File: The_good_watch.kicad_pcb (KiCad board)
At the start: 2 copper layers, 45 x 45 mm, 38 parts, among them IC1 DW01A, J1 Main, J2 USB_C_Receptacle_USB2.0, J3 PROG, J4 Screen, J5 Button, M1 Motor_DC, Q1 FS8205A, SW1 SW_Push, SW2 SW_Push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

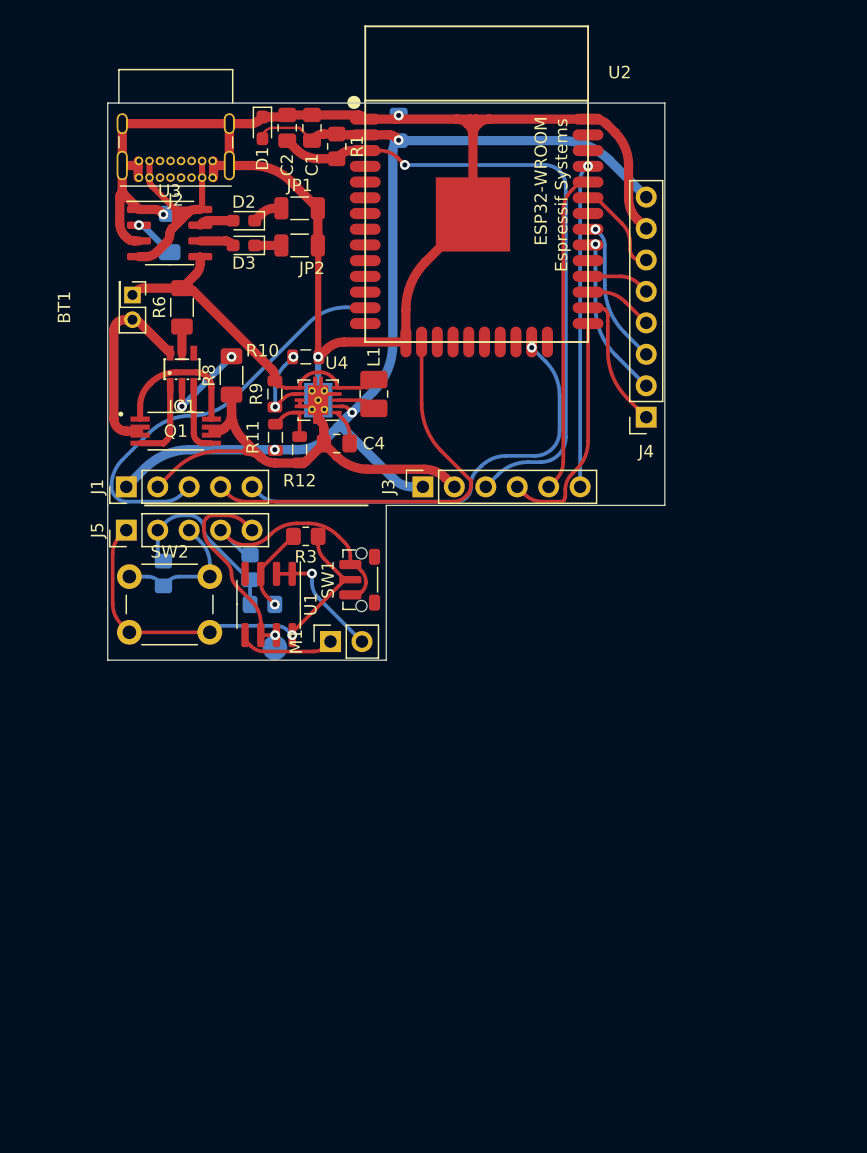
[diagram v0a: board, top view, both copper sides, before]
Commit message: Connector layout trial
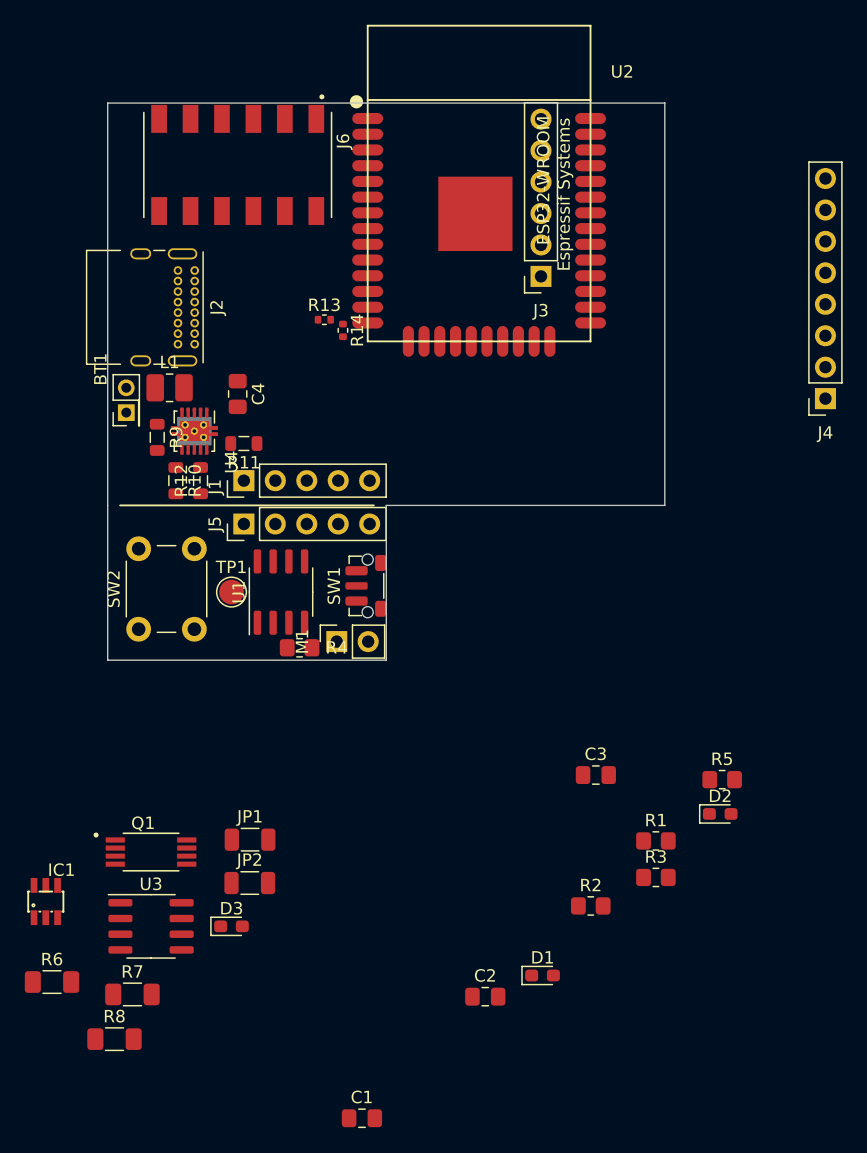
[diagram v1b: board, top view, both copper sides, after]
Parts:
- added J6: 70AAJ-6-M0G, 70AAJ-6-M0G:BOURNS_70AAJ-6-M0G, F.Cu at (110.5, 55.0)
- added R13: 442K, Resistor_SMD:R_0402_1005Metric, F.Cu at (117.5, 67.5)
- added R14: 160K, Resistor_SMD:R_0402_1005Metric, F.Cu at (119.0, 68.4)
- C3, R2, R4, R5, R7, TP1: moved to F.Cu
- moved C1 80.1 mm to (120.5, 132.0), turned to 0 degrees
- moved D1 72.1 mm to (135.1, 120.5), turned to 0 degrees
- moved C2 72.0 mm to (130.5, 122.2), turned to 0 degrees
- moved R1 61.7 mm to (144.3, 109.6), turned to 0 degrees
- moved R7 61.6 mm to (102.0, 122.0), turned to 0 degrees
- moved D2 61.5 mm to (149.5, 107.4), turned to 0 degrees
- moved U3 56.0 mm to (103.5, 116.5)
- moved R6 55.5 mm to (95.5, 121.0), turned to 0 degrees
- moved D3 55.0 mm to (110.0, 116.5), turned to 0 degrees
- moved C3 54.7 mm to (139.4, 104.3), turned to 0 degrees
- moved R8 54.4 mm to (100.5, 125.6), turned to 0 degrees
- moved JP2 51.7 mm to (111.5, 113.0), turned to 0 degrees
- moved JP1 51.2 mm to (111.5, 109.5)
- moved R5 48.1 mm to (149.6, 104.7), turned to 0 degrees
- moved IC1 44.4 mm to (95.0, 114.5)
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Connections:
- net SDA renamed MOSI
- U2 pad 14: unconnected-(U2-Pad14) -> IO12
- U2 pad 36: unconnected-(U2-Pad36) -> MISO
- U2 pad 8: unconnected-(U2-Pad8) -> ANALOG
- U2 pad 9: unconnected-(U2-Pad9) -> SENSE
- U4 pad 6: +BATT -> Net-(U4-Pad6)
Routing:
- net GND: track 188.8 -> 0.00 mm, vias 3 -> 0
- net +3V3: track 123.4 -> 0.00 mm, vias 4 -> 0
- net EN: track 53.0 -> 0.00 mm, vias 1 -> 0
- net M_OUT_M: track 35.8 -> 0.00 mm, vias 1 -> 0
- net B1_M: track 34.3 -> 0.00 mm
- net B2_M: track 33.9 -> 0.00 mm
- net +BATT: track 28.3 -> 0.00 mm
- net TXD: track 26.1 -> 0.00 mm, vias 1 -> 0
- net RXD: track 26.1 -> 0.00 mm
- net VCC_IN: track 22.8 -> 0.00 mm
- net B1: track 20.3 -> 0.00 mm
- net IO0: track 19.0 -> 0.00 mm
- net M_OUT: track 17.5 -> 0.00 mm, vias 1 -> 0
- net -BATT: track 15.8 -> 0.00 mm
- net SCK: track 12.9 -> 0.00 mm, vias 1 -> 0
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
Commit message: Finished layout and routing
Only minor graphical cleanup remains
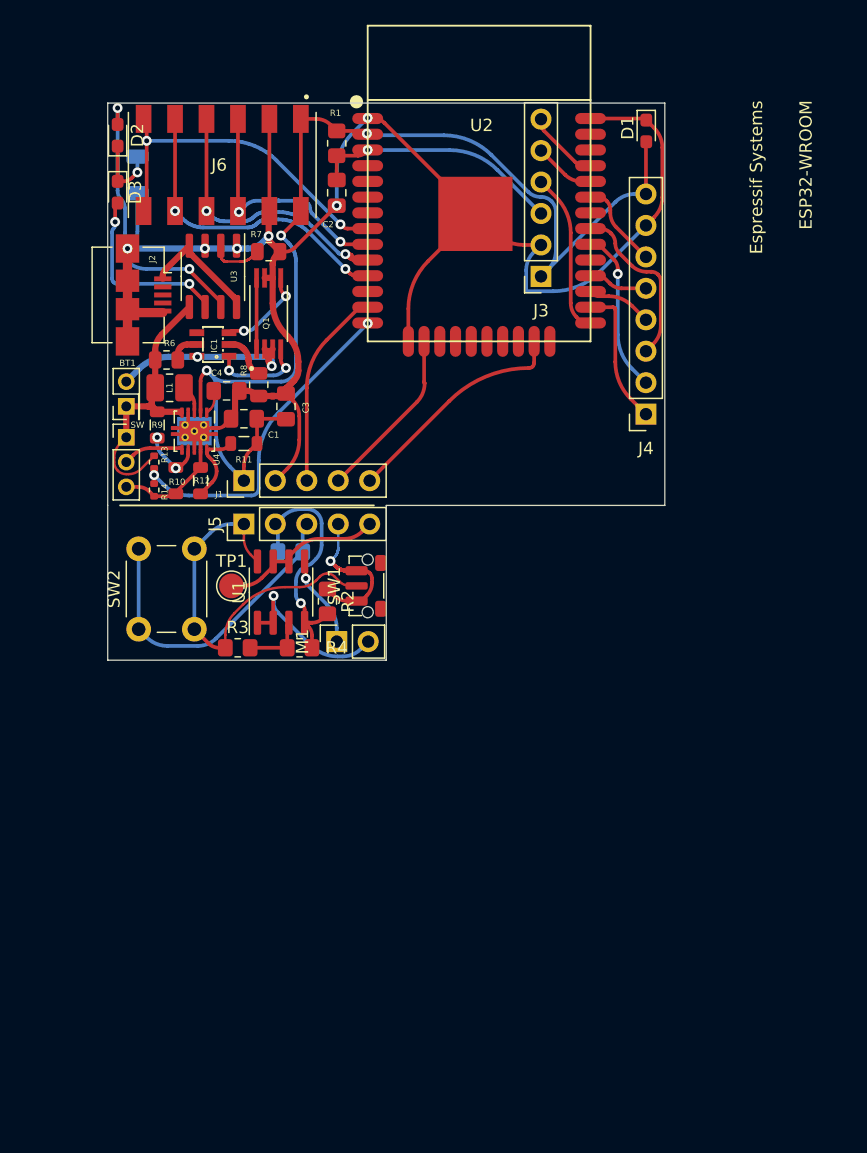
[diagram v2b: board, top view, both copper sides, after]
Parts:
- removed JP2: STBY, Capacitor_SMD:C_1206_3216Metric
- added SW: SW_SPDT, Connector_PinHeader_2.00mm:PinHeader_1x03_P2.00mm_Vertical, F.Cu at (101.5, 77.0)
- J2: value USB_C_Receptacle_USB2.0 -> USB_B_Micro; footprint Connector_USB:USB_C_Receptacle_GCT_USB4085 -> Connector_USB:USB_Micro-B_Amphenol_10104110_Horizontal
- JP1, R5: moved to B.Cu
- R6, R7, R8: footprint Resistor_SMD:R_1206_3216Metric_Pad1.30x1.75mm_HandSolder -> Resistor_SMD:R_0805_2012Metric
- moved D2 73.3 mm to (100.8, 52.6), turned to 90 degrees
- moved D1 68.7 mm to (143.5, 52.2), turned to -90 degrees
- moved C2 66.0 mm to (118.5, 57.2), turned to -90 degrees
- moved R1 62.0 mm to (118.5, 53.2), turned to -90 degrees
- moved R7 61.0 mm to (113.0, 62.0)
- moved D3 60.0 mm to (100.8, 57.2), turned to -90 degrees
- moved C1 57.3 mm to (111.0, 75.5), turned to 180 degrees
- moved JP1 54.5 mm to (102.4, 55.8), turned to -90 degrees
- moved R8 54.1 mm to (112.2, 72.8), turned to 90 degrees
- moved U3 52.7 mm to (108.5, 64.0), turned to -90 degrees
- moved R6 51.1 mm to (104.8, 70.8), turned to 180 degrees
- moved IC1 47.0 mm to (108.5, 69.5), turned to 90 degrees
- moved Q1 44.5 mm to (113.0, 67.0), turned to 90 degrees
- moved R5 39.4 mm to (114.8, 86.2), turned to 180 degrees
- moved C3 38.9 mm to (114.4, 74.5), turned to 90 degrees
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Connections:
- D3 pad 1: Net-(D3-Pad1) -> Net-(D2-Pad1)
- R13 pad 1: BATT+ -> +BATT
- U2 pad 10: unconnected-(U2-Pad10) -> SDA
- U2 pad 11: unconnected-(U2-Pad11) -> SCL
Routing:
- net GND: track 0.00 -> 180.7 mm, vias 0 -> 7
- net +3V3: track 0.00 -> 124.7 mm, vias 0 -> 3
- net ANALOG: track 0.00 -> 28.2 mm, vias 0 -> 2
- net IO12: track 0.00 -> 27.2 mm, vias 0 -> 2
- net B2: track 0.00 -> 25.5 mm
- net SCL: track 0.00 -> 25.3 mm, vias 0 -> 2
- net +BATT: track 0.00 -> 23.6 mm
- net Net-(D2-Pad2): track 0.00 -> 23.5 mm, vias 0 -> 2
- net SDA: track 0.00 -> 23.0 mm, vias 0 -> 2
- net EN: track 0.00 -> 20.5 mm, vias 0 -> 1
- net SENSE: track 0.00 -> 19.8 mm, vias 0 -> 2
- net M_OUT_M: track 0.00 -> 18.6 mm
- net B2_M: track 0.00 -> 16.1 mm
- net -BATT: track 0.00 -> 15.6 mm, vias 0 -> 2
- net Net-(D3-Pad2): track 0.00 -> 15.5 mm, vias 0 -> 2
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
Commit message: Added copper fill
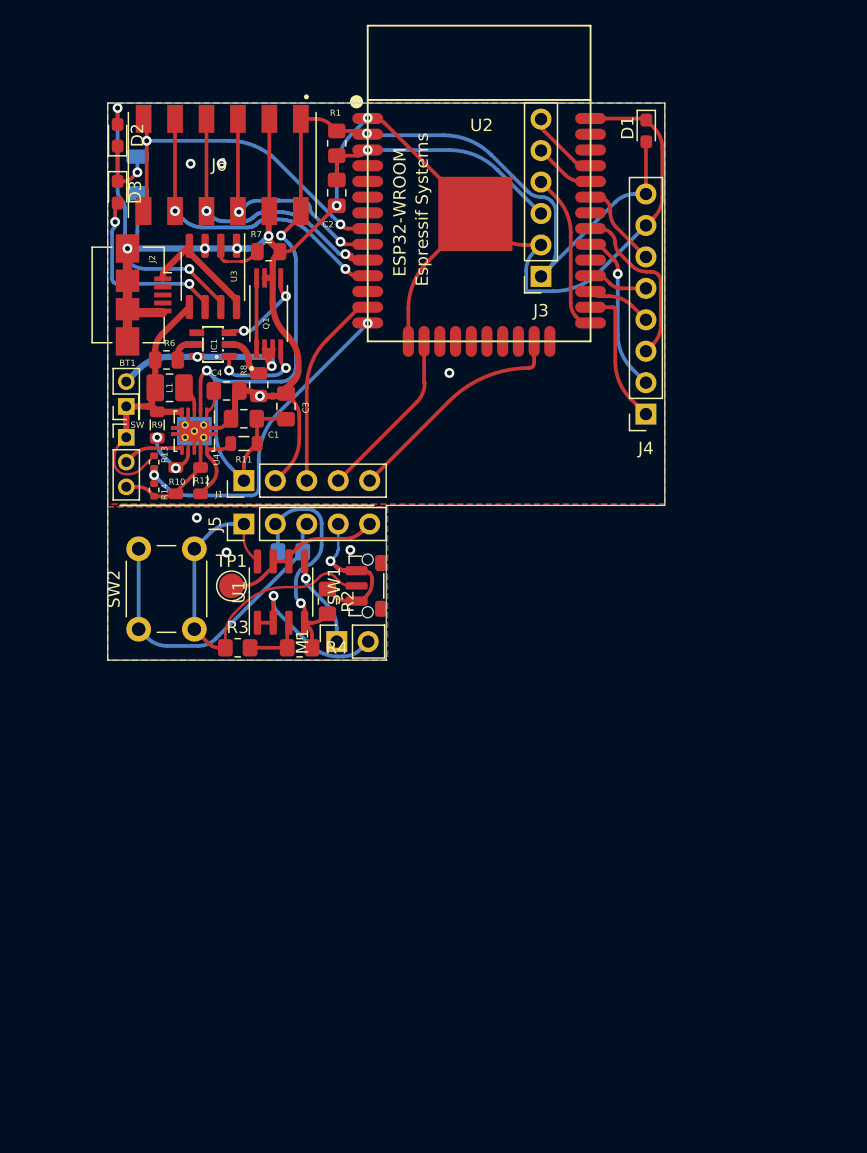
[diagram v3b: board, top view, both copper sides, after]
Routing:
- net GND: vias 7 -> 14
- added copper zone on B.Cu, net GND
- added copper zone on F.Cu, net GND
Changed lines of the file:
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@@
       (effects (font (size 1 1) (thickness 0.15)))
     )
-    (fp_text user "Espressif Systems" (at -22.4 0.5 90) (layer "F.SilkS")
+    (fp_text user "Espressif Systems" (at 4.6 -2.1 90) (layer "F.SilkS")
       (effects (font (size 1 1) (thickness 0.15)))
     )
-    (fp_text user "ESP32-WROOM" (at -26.4 1.5 90) (layer "F.SilkS")
+    (fp_text user "ESP32-WROOM" (at 6.4 -2.3 90) (layer "F.SilkS")
       (effects (font (size 1 1) (thickness 0.15)))
     )
@@
   (segment (start 112.318882 73.6625) (end 112.318573 73.6625) (width 0.5) (layer "F.Cu") (net 46))
   (segment (start 112.359069 73.6625) (end 112.358451 73.6625) (width 0.5) (layer "F.Cu") (net 46))
+  (via (at 119.6 86.1) (size 0.8) (drill 0.4) (layers "F.Cu" "B.Cu") (free) (net 46))
+  (via (at 109.6 86.3) (size 0.8) (drill 0.4) (layers "F.Cu" "B.Cu") (free) (net 46))
+  (via (at 106.7 54.9) (size 0.8) (drill 0.4) (layers "F.Cu" "B.Cu") (free) (net 46))
+  (via (at 112.291681 73.6625) (size 0.8) (drill 0.4) (layers "F.Cu" "B.Cu") (net 46))
+  (via (at 107.2 83.5) (size 0.8) (drill 0.4) (layers "F.Cu" "B.Cu") (free) (net 46))
   (via (at 115.6 90.4) (size 0.8) (drill 0.4) (layers "F.Cu" "B.Cu") (net 46))
+  (via (at 109.2 54.9) (size 0.8) (drill 0.4) (layers "F.Cu" "B.Cu") (free) (net 46))
   (via (at 113 60.75) (size 0.8) (drill 0.4) (layers "F.Cu" "B.Cu") (net 46))
   (via (at 101.6 61.75) (size 0.8) (drill 0.4) (layers "F.Cu" "B.Cu") (net 46))
   (via (at 121 51.2) (size 0.8) (drill 0.4) (layers "F.Cu" "B.Cu") (net 46))
+  (via (at 127.6 71.8) (size 0.8) (drill 0.4) (layers "F.Cu" "B.Cu") (free) (net 46))
   (via (at 110.45 61.75) (size 0.8) (drill 0.4) (layers "F.Cu" "B.Cu") (net 46))
   (via (at 118.5 58.2875) (size 0.8) (drill 0.4) (layers "F.Cu" "B.Cu") (net 46))
@@
   (arc (start 111.611023 81.699511) (mid 112.027147 81.527147) (end 112.199511 81.111023) (width 0.3) (layer "B.Cu") (net 59))
   (arc (start 104.574755 80.874755) (mid 105.488296 81.485163) (end 106.565891 81.699511) (width 0.3) (layer "B.Cu") (net 59))
+  (zone (net 46) (net_name "GND") (layers F&B.Cu) (hatch edge 0.508)
+    (connect_pads (clearance 0.254))
+    (min_thickness 0.254) (filled_areas_thickness no)
+    (fill yes (thermal_gap 0.508) (thermal_bridge_width 0.508) (island_removal_mode 2) (island_area_min 5))
+    (polygon
+      (pts
+        (xy 122.6 95)
+        (xy 100 95)
+        (xy 100 82.6)
+        (xy 122.6 82.6)
+      )
+    )
+  )
+  (zone (net 46) (net_name "GND") (layers F&B.Cu) (hatch edge 0.508)
+    (connect_pads (clearance 0.508))
+    (min_thickness 0.254) (filled_areas_thickness no)
+    (fill yes (thermal_gap 0.508) (thermal_bridge_width 0.508) (island_removal_mode 2) (island_area_min 5))
+    (polygon
+      (pts
+        (xy 145 82.4)
+        (xy 100 82.4)
+        (xy 100 50)
+        (xy 145 50)
+      )
+    )
+  )
 )

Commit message: Added graphics
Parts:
- added REF**: OSHW-Logo2_9.8x8mm_SilkScreen, Symbol:OSHW-Logo2_9.8x8mm_SilkScreen, F.Cu at (138.5, 77.6)
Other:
- board text added: "https://github.com/ Thecactusman0/ OSSM_MKIII"
